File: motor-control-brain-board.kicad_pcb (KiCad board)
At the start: 4 copper layers, 60 x 50 mm, 107 parts, among them J1 GPIO, J10 PWM, J11 PWR, J12 POWER_SENSE, J13 MISC_SENSE, J2 I2C, J3 SERIAL_1, J4 SERIAL_2, J5 CAN, J6 SPI, J7 USB_C_Receptacle_USB2.0_16P, J8 SWD, J9 POS_SENSE, SW1 RST, U1 TLV76750QWDRBxQ1, U10 TLV6001DCK, U11 TLV6001DCK, U12 TLV6001DCK, U2 TLV76733QWDRBxQ1, U3 M95256-RDW6TP, U4 STM32G474RETx, U5 TCAN1044V-Q1, U6 TLV6001DCK, U7 TLV6001DCK, U8 TLV6001DCK, U9 TLV6001DCK

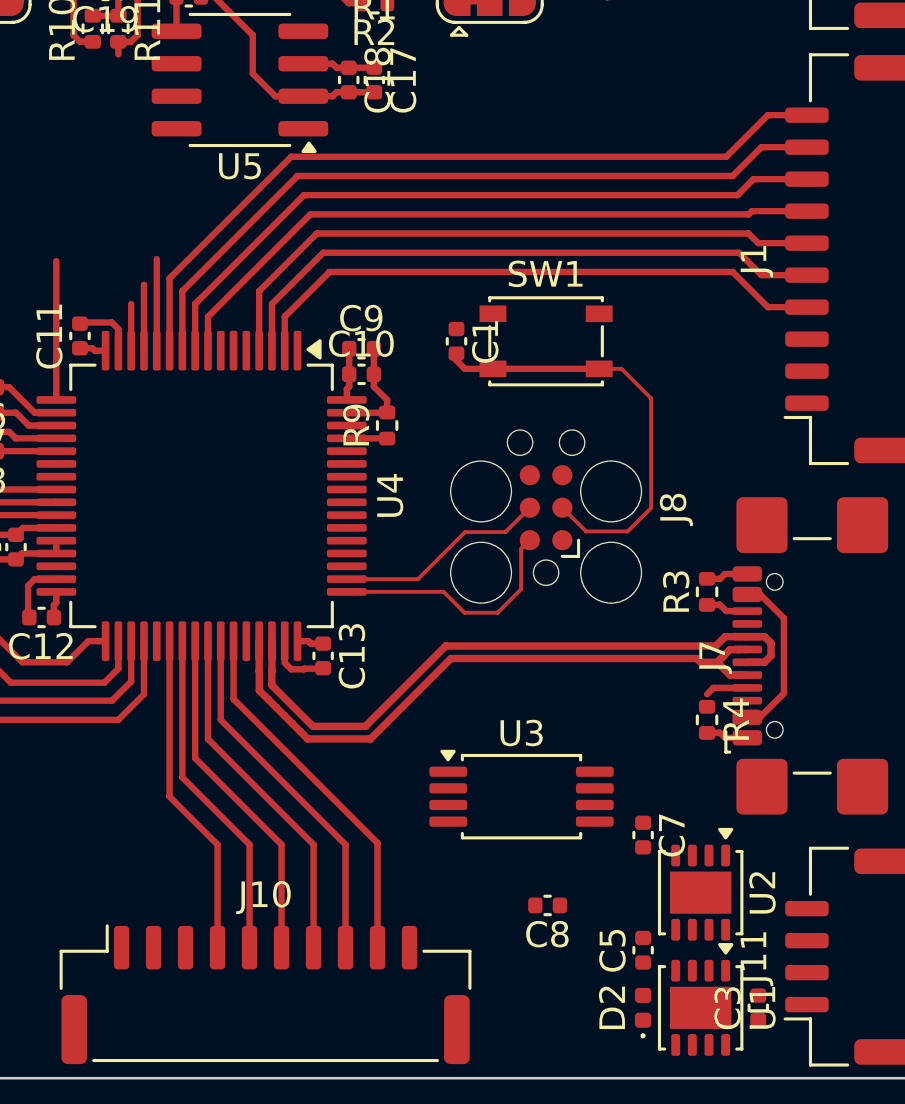
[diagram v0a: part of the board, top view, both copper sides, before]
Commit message: Changed to LPUART for 1 channel to improve routing etc. Can now add 1 more ADC as needed. Todo: Figure out GPIO and add oscillator
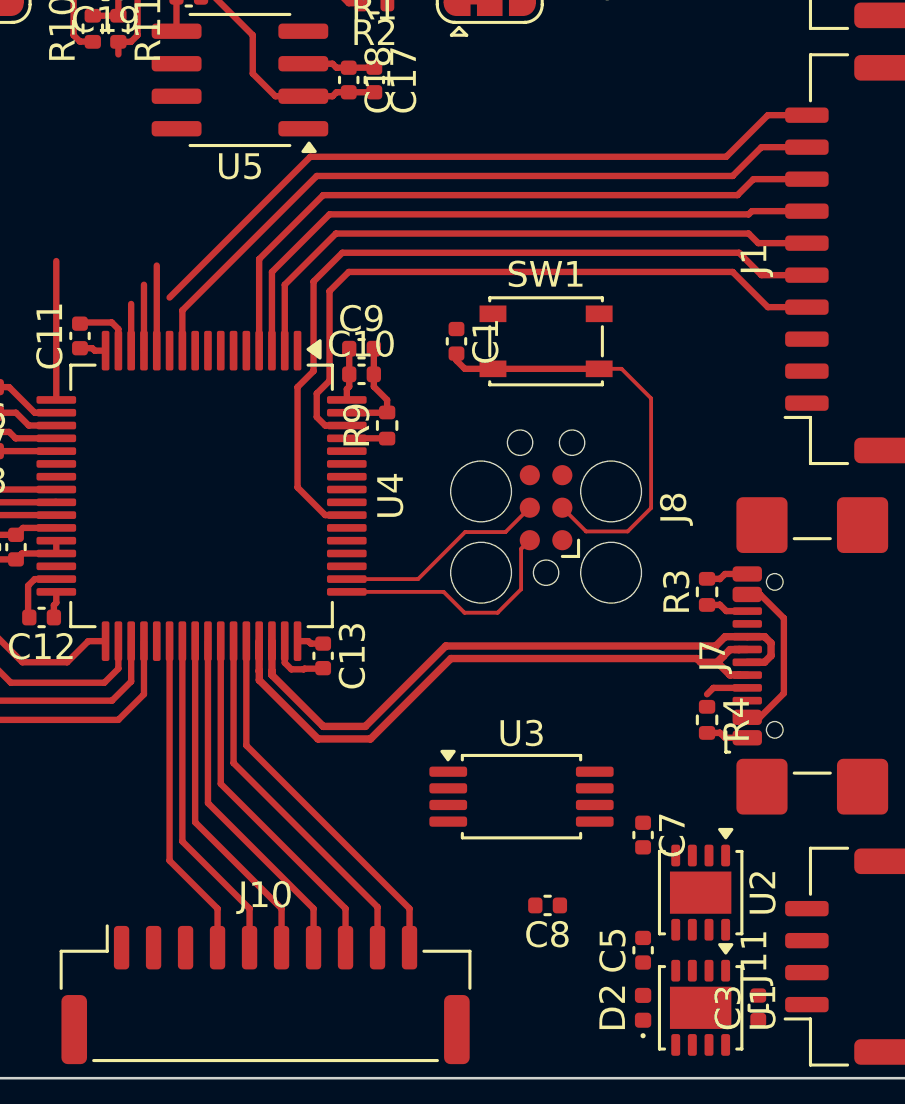
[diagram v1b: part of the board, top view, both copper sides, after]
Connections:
- net /I2C_SDA renamed /I2C1_SDA
- net /Motor_ADC_Buffer/CURR_A_V+ renamed /Power_ADC_Buffer/CURR_A_V+
- net /Motor_ADC_Buffer/CURR_A_V- renamed /Power_ADC_Buffer/CURR_A_V-
- net /Motor_ADC_Buffer/CURR_B_V+ renamed /Power_ADC_Buffer/CURR_B_V+
- net /Motor_ADC_Buffer/CURR_B_V- renamed /Power_ADC_Buffer/CURR_B_V-
- net /Motor_ADC_Buffer/CURR_C_V+ renamed /Power_ADC_Buffer/CURR_C_V+
- net /Motor_ADC_Buffer/CURR_C_V- renamed /Power_ADC_Buffer/CURR_C_V-
- net /Motor_ADC_Buffer/VOLT_DC_V+ renamed /Power_ADC_Buffer/VOLT_DC_V+
- net /Motor_ADC_Buffer/VOLT_DC_V- renamed /Power_ADC_Buffer/VOLT_DC_V-
- net /SPI_MISO renamed /SPI1_MISO
- net /SPI_MOSI renamed /SPI1_MOSI
- net /SPI_NSS renamed /SPI1_NSS
- net /SPI_SCK renamed /SPI1_SCK
- J2 pad 4: /I2C_SCL -> /I2C1_SCL
- J3 pad 3: /UART1_TX -> /LPUART1_TX
- J3 pad 4: /UART1_RX -> /LPUART1_RX
- J8 pad 6: unconnected-(J8-Pin_6-Pad6) -> /UART2_TX
- R2 pad 2: /I2C_SCL -> /I2C1_SCL
- U3 pad 1: /MCU/SPI2_NSS -> /MCU/SPI3_NSS
- U3 pad 2: /MCU/SPI2_MISO -> /MCU/SPI3_MISO
- U3 pad 5: /MCU/SPI2_MOSI -> /MCU/SPI3_MOSI
- U3 pad 6: /MCU/SPI2_SCK -> /MCU/SPI3_SCK
- U4 pad 2: /GPIO_1 -> /GPIO_3
- U4 pad 22: /UART1_TX -> /I2C1_SCL
- U4 pad 23: /UART1_RX -> unconnected-(U4-PC5-Pad23)
- U4 pad 3: /GPIO_2 -> /GPIO_4
- U4 pad 37: /MCU/SPI2_MOSI -> unconnected-(U4-PB15-Pad37)
- U4 pad 4: /GPIO_3 -> /GPIO_5
- U4 pad 44: /MCU/SPI2_MISO -> /PWM_EN
- U4 pad 5: /MCU/SPI2_NSS -> /MCU/OSC_IN
- U4 pad 51: /I2C_SCL -> /MCU/SPI3_NSS
- U4 pad 52: unconnected-(U4-PC10-Pad52) -> /MCU/SPI3_SCK
- U4 pad 53: unconnected-(U4-PC11-Pad53) -> /MCU/SPI3_MISO
- U4 pad 54: unconnected-(U4-PC12-Pad54) -> /MCU/SPI3_MOSI
- U4 pad 55: /PWM_EN -> /GPIO_2
- U4 pad 6: /MCU/SPI2_SCK -> /MCU/OSC_OUT
- U4 pad 62: unconnected-(U4-PB9-Pad62) -> /GPIO_1
- U4 pad 8: /GPIO_4 -> /LPUART1_RX
- U4 pad 9: /GPIO_5 -> /LPUART1_TX
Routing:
- net /PWM_EN: track 0.00 -> 14.6 mm
- net /GPIO_2: track 23.9 -> 30.8 mm
- net /I2C_SCL: track 3.65 -> 0.00 mm
- net /I2C1_SCL: track 0.00 -> 3.65 mm
- net /GPIO_1: track 23.0 -> 26.0 mm
- net /GPIO_7: track 30.4 -> 27.9 mm
- net /GPIO_5: track 27.7 -> 26.3 mm
- net /GPIO_4: track 26.4 -> 25.0 mm
- net /GPIO_3: track 24.8 -> 24.0 mm

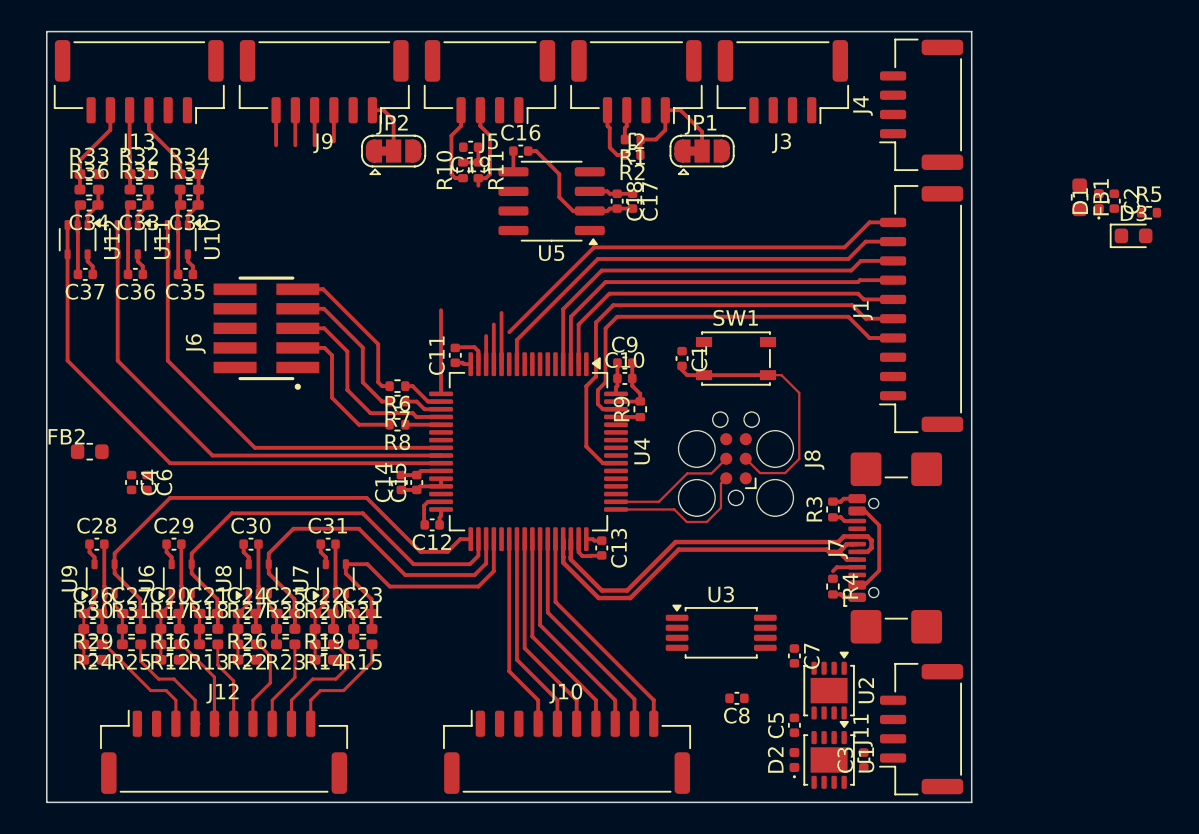
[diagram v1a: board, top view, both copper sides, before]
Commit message: Figured out GPIO and added oscillator to schematic, need to pick part
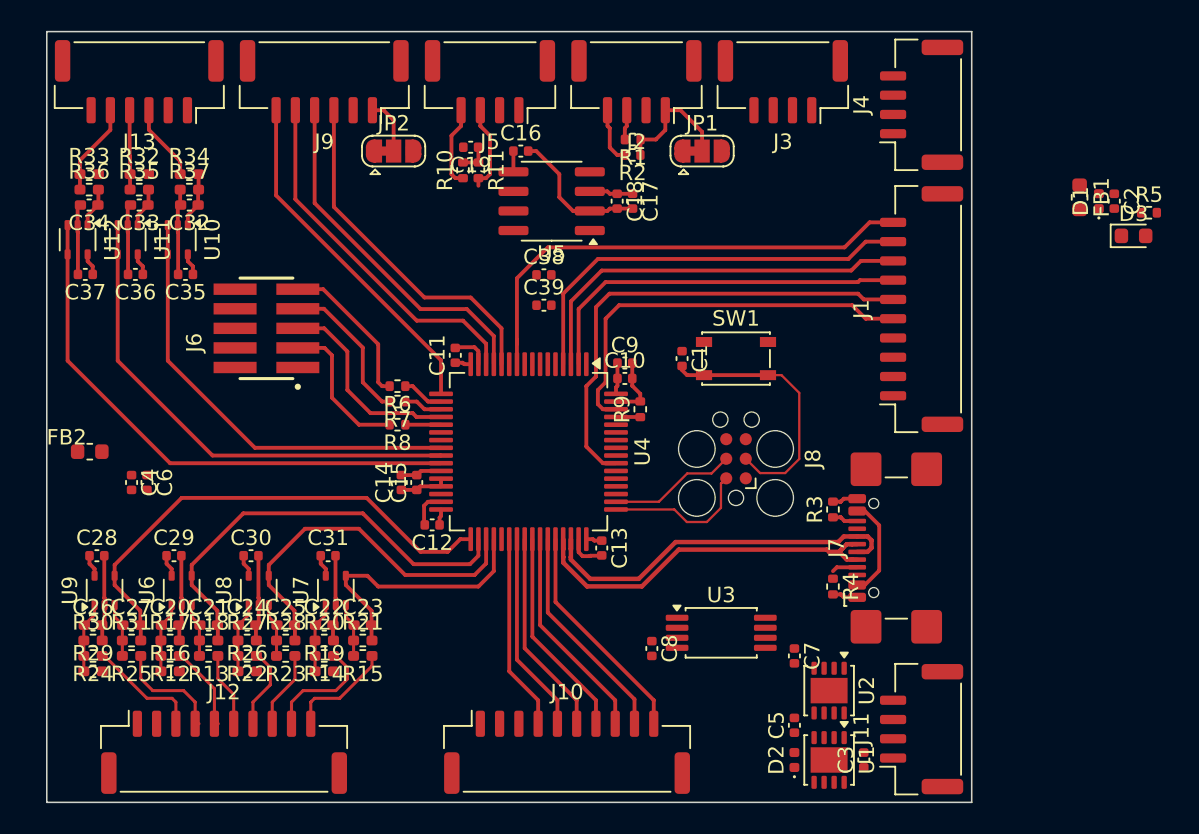
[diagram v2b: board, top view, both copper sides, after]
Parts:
- added C38: c, Capacitor_SMD:C_0402_1005Metric, F.Cu at (152.2, 85.8)
- added C39: c, Capacitor_SMD:C_0402_1005Metric, F.Cu at (152.2, 87.8)
- moved C8 6.40 mm to (159.2, 110.0), turned to -90 degrees
- moved C20 0.75 mm to (128.0, 108.5)
- moved C21 0.75 mm to (130.5, 108.5)
- moved C22 0.75 mm to (138.0, 108.5)
- moved C23 0.75 mm to (140.5, 108.5)
- moved C24 0.75 mm to (133.0, 108.5)
- moved C25 0.75 mm to (135.5, 108.5)
- moved C26 0.75 mm to (123.0, 108.5)
- moved C27 0.75 mm to (125.5, 108.5)
- moved C28 0.75 mm to (123.2, 104.0)
- moved C29 0.75 mm to (128.2, 104.0)
- moved C30 0.75 mm to (133.2, 104.0)
- moved C31 0.75 mm to (138.2, 104.0)
- moved R12 0.75 mm to (128.0, 110.5)
- moved R13 0.75 mm to (130.5, 110.5)
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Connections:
- J1 pad 1: +5V -> +12V
- J1 pad 10: /GPIO_7 -> /GPIO_6
- J1 pad 2: +3V3 -> +5V
- J1 pad 3: GND -> +3V3
- J1 pad 4: /GPIO_1 -> GND
- J1 pad 5: /GPIO_2 -> /GPIO_1
- J1 pad 6: /GPIO_3 -> /GPIO_2
- J1 pad 7: /GPIO_4 -> /GPIO_3
- J1 pad 8: /GPIO_5 -> /GPIO_4
- J1 pad 9: /GPIO_6 -> /GPIO_5
- U4 pad 11: /GPIO_7 -> unconnected-(U4-PC3-Pad11)
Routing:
- net /GPIO_7: track 27.9 -> 0.00 mm
- net /POS_C/RES_OUT: track 4.10 -> 23.4 mm
- net /POS_B: track 4.85 -> 23.0 mm
- net /POS_A: track 5.35 -> 22.7 mm
- net /POS_Z: track 7.70 -> 22.8 mm
- net /GPIO_6: track 28.6 -> 31.7 mm
- net /GPIO_5: track 26.3 -> 27.4 mm
- net /GPIO_4: track 25.0 -> 26.1 mm
- net /GPIO_3: track 24.0 -> 24.8 mm
- net /CURR_B-: track 5.76 -> 5.01 mm
- net /CURR_B+: track 6.08 -> 5.33 mm
- net /CURR_A-: track 5.58 -> 4.83 mm
- net /CURR_A+: track 6.22 -> 5.47 mm
- net /GPIO_2: track 30.8 -> 31.5 mm
- net /CURR_C-: track 7.67 -> 7.00 mm
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
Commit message: Moved MCU to make more room for routing, updated crystal package/PN
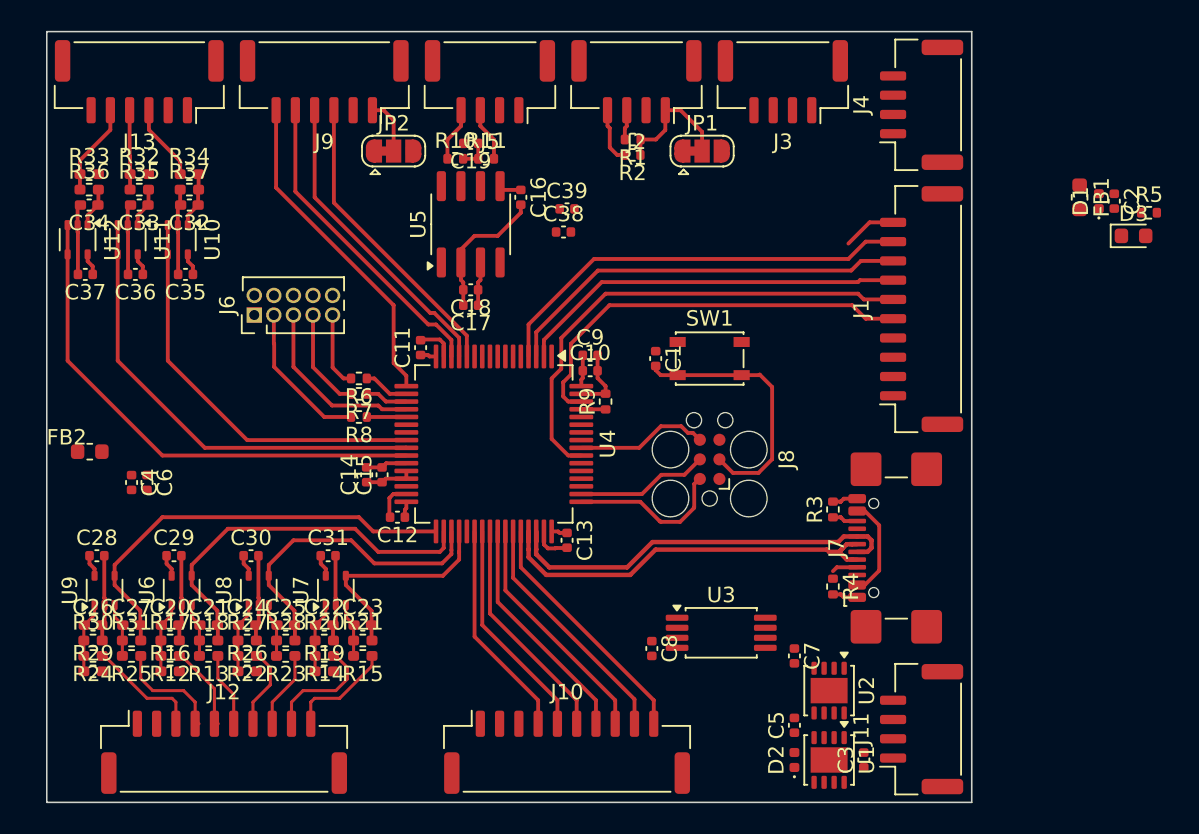
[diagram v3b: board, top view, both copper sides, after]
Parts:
- C38, C39: value c -> 30p
- J6: footprint User_Connector:Samtec_FTSH-105-XX-X-DV-K -> Connector_PinHeader_1.27mm:PinHeader_2x05_P1.27mm_Vertical
- moved C17 12.5 mm to (147.5, 87.8), turned to 180 degrees
- moved C18 11.1 mm to (147.5, 86.8), turned to 180 degrees
- moved C39 6.43 mm to (153.8, 81.5)
- moved U5 5.46 mm to (147.5, 82.5), turned to 90 degrees
- moved C38 3.06 mm to (153.5, 83.0)
- moved C16 3.00 mm to (150.8, 80.8), turned to -90 degrees
- moved R6 2.55 mm to (140.2, 92.5)
- moved R7 2.55 mm to (140.2, 93.5)
- moved R8 2.55 mm to (140.2, 95.0)
- moved C10 2.30 mm to (155.2, 92.0)
- moved C11 2.30 mm to (144.2, 90.5)
- moved C12 2.30 mm to (142.8, 101.5)
- moved C13 2.30 mm to (153.8, 103.0)
- moved C14 2.30 mm to (140.8, 98.8)
- moved C15 2.30 mm to (141.8, 98.8)
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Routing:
- net /GPIO_6: track 31.7 -> 3.47 mm
- net /UART2_TX: track 0.00 -> 8.63 mm
- net /SPI1_NSS: track 10.0 -> 4.90 mm
- net /VOLT_DC: track 32.3 -> 28.1 mm
- net /CURR_A: track 28.3 -> 24.7 mm
- net /CURR_B: track 23.8 -> 20.5 mm
- net /SPI1_SCK: track 9.77 -> 6.57 mm
- net /POS_A: track 22.7 -> 19.5 mm
- net /POS_B: track 23.0 -> 20.1 mm
- net /POS_C/RES_OUT: track 23.4 -> 20.5 mm
- net /CURR_C: track 17.3 -> 14.5 mm
- net /THM_1: track 32.4 -> 29.9 mm
- net /THM_2: track 35.8 -> 33.3 mm
- net /ACC: track 28.9 -> 26.4 mm
- net /CANL: track 5.76 -> 3.52 mm
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
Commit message: Routing
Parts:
- added Y1: ECS-160-20-33-DU-TR, Oscillator:Oscillator_SMD_Abracon_ASE-4Pin_3.2x2.5mm, F.Cu at (158.2, 83.8)
- U5: footprint Package_SO:SOIC-8_3.9x4.9mm_P1.27mm -> Package_TO_SOT_SMD:TSOT-23-8
- moved C39 7.59 mm to (161.0, 83.8), turned to -90 degrees
- moved C17 2.75 mm to (147.5, 85.0)
- moved C18 2.75 mm to (147.5, 84.0)
- moved C8 2.25 mm to (159.2, 107.8)
- moved U3 2.25 mm to (163.8, 106.8)
- moved C38 2.12 mm to (155.5, 83.8), turned to 90 degrees
- moved U5 1.25 mm to (147.5, 81.2)
- moved C16 1.00 mm to (149.8, 80.8)
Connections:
- J3 pad 3: /LPUART1_TX -> /LPUART1_RX
- J3 pad 4: /LPUART1_RX -> /LPUART1_TX
- J4 pad 3: /UART2_TX -> /UART2_RX
- J4 pad 4: /UART2_RX -> /UART2_TX
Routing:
- net /LPUART1_RX: track 0.00 -> 29.7 mm
- net /LPUART1_TX: track 0.00 -> 29.4 mm
- net /MCU/OSC_OUT: track 0.00 -> 18.1 mm
- net /MCU/OSC_IN: track 0.00 -> 11.7 mm
- net GND: track 64.2 -> 67.5 mm
- net /CANL: track 3.52 -> 6.16 mm
- net /CANH: track 3.52 -> 6.16 mm
- net /GPIO_1: track 27.2 -> 26.5 mm
